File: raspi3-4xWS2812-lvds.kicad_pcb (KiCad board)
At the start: 2 copper layers, 28.5 x 51.2 mm, 41 parts, among them J1 Conn_ARM_JTAG_SWD_10, J2 Raspberry_Pi_2_3, J3 Conn_02x08_Odd_Even, J4 Conn_02x04_Odd_Even, J5 Conn_01x02, U1 SAMC21G17A-A, U2 SN65LVDS047D, U3 TJA1049T-3, U4 74LS32, Y1 8MHz

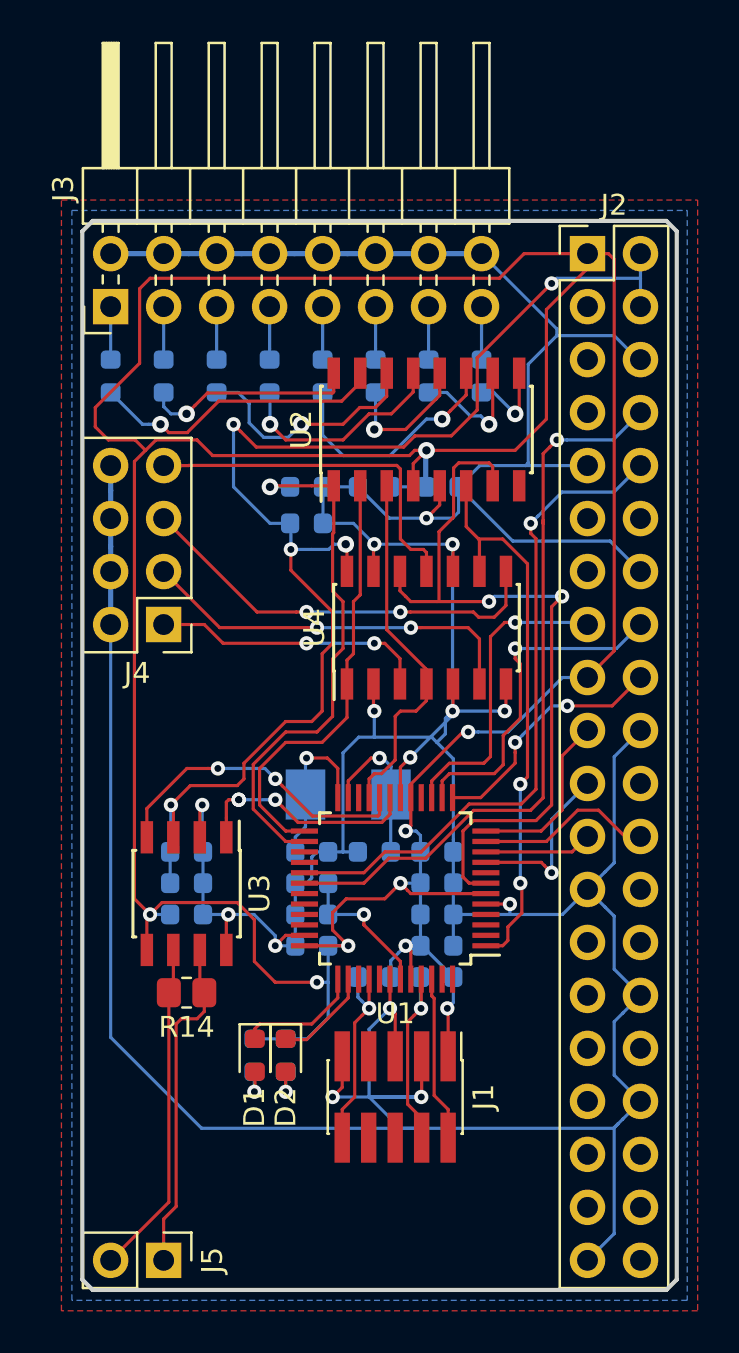
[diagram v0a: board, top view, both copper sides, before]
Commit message: improve silkscreen, make jtag connector through hole
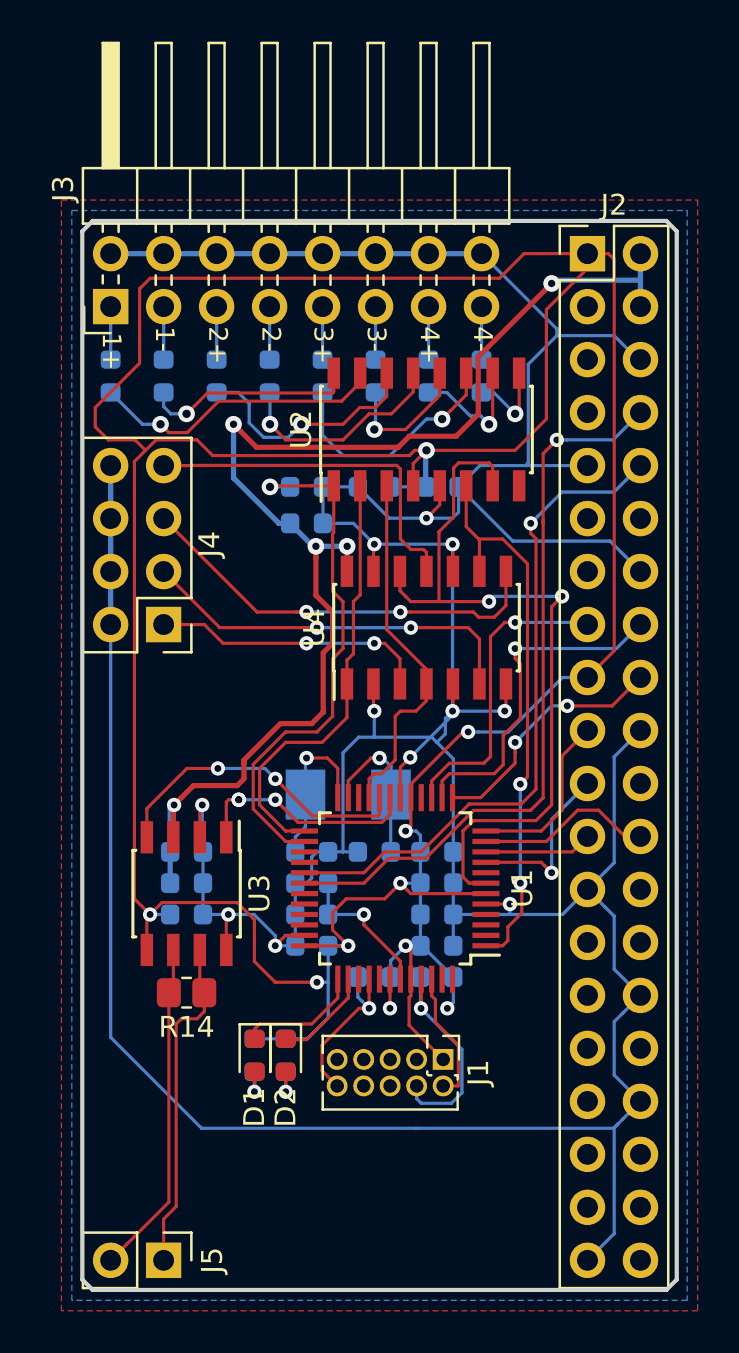
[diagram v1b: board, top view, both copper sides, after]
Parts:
- J1: footprint Connector_PinHeader_1.27mm:PinHeader_2x05_P1.27mm_Vertical_SMD -> Connector_PinHeader_1.27mm:PinHeader_2x05_P1.27mm_Vertical
- moved J1 2.92 mm to (102.3, 90.7)
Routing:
- net GND: track 252.0 -> 231.2 mm, vias 14 -> 12
- net +3V3: track 177.6 -> 179.9 mm
- net +5V: track 62.8 -> 64.7 mm
- net SWDIO: track 7.93 -> 6.37 mm
- net NRST: track 9.86 -> 8.36 mm
- net SWCLK: track 9.66 -> 10.9 mm
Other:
- net class 0,25 added: clearance 0.1524, trace_width 0.25, via_dia 0.8, via_drill 0.35
- board text added: "1+"
- board text added: "1-"
- board text added: "2+"
- board text added: "2-"
- board text added: "3+"
- board text added: "3-"
- board text added: "4+"
- board text added: "4-"
- board text added: "4x LVDS WS2812 raspi hat v0.1 https://bytewerk.org/"
